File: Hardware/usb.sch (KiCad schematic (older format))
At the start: 13 parts

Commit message: Selected some footprints
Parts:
- P?: footprint (none) -> Connector_USB:USB_C_Receptacle_GCT_USB4085
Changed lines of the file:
@@
 F 0 "P?" H 3857 4567 50  0000 C CNN
 F 1 "USB_C_Plug_USB2.0" H 3857 4476 50  0000 C CNN
-F 2 "" H 3900 3700 50  0001 C CNN
+F 2 "Connector_USB:USB_C_Receptacle_GCT_USB4085" H 3900 3700 50  0001 C CNN
 F 3 "https://www.usb.org/sites/default/files/documents/usb_type-c.zip" H 3900 3700 50  0001 C CNN
 	1    3750 3700

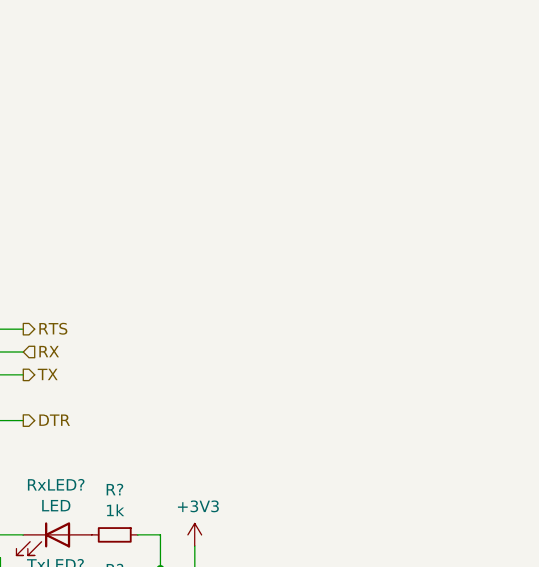
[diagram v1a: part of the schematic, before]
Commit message: Added test points everywhere
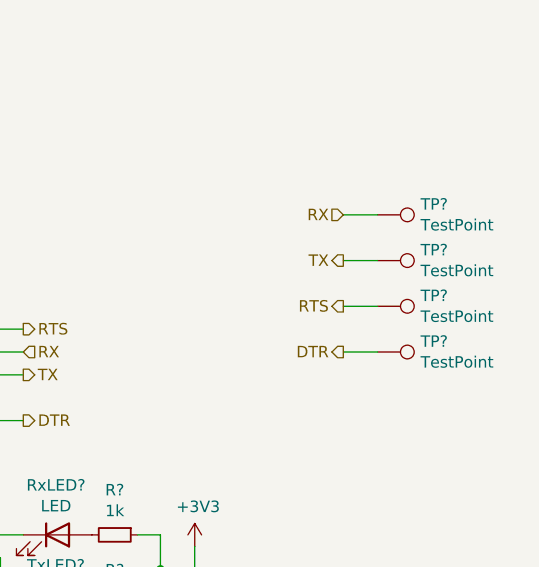
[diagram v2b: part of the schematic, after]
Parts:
- added TP? (x4): TestPoint, symbol Connector:TestPoint
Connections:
- net DTR: now also TP?.1
- net RTS: now also TP?.1
- net RX: now also TP?.1
- net TX: now also TP?.1
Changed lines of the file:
@@
 $Descr A4 11693 8268
 encoding utf-8
-Sheet 4 4
+Sheet 4 5
 Title ""
 Date ""
@@
 Text HLabel 7650 3750 2    50   Output ~ 0
 DTR
+$Comp
+L Connector:TestPoint TP?
+U 1 1 607C08D3
+P 9200 2850
+F 0 "TP?" V 9154 3038 50  0000 L CNN
+F 1 "TestPoint" V 9245 3038 50  0000 L CNN
+F 2 "" H 9400 2850 50  0001 C CNN
+F 3 "~" H 9400 2850 50  0001 C CNN
+	1    9200 2850
+	0    1    1    0
+$EndComp
+$Comp
+L Connector:TestPoint TP?
+U 1 1 607C0C71
+P 9200 3050
+F 0 "TP?" V 9154 3238 50  0000 L CNN
+F 1 "TestPoint" V 9245 3238 50  0000 L CNN
+F 2 "" H 9400 3050 50  0001 C CNN
+F 3 "~" H 9400 3050 50  0001 C CNN
+	1    9200 3050
+	0    1    1    0
+$EndComp
+Wire Wire Line
+	9200 2850 9050 2850
+Wire Wire Line
+	9200 3050 9050 3050
+$Comp
+L Connector:TestPoint TP?
+U 1 1 607C5A06
+P 9200 3250
+F 0 "TP?" V 9154 3438 50  0000 L CNN
+F 1 "TestPoint" V 9245 3438 50  0000 L CNN
+F 2 "" H 9400 3250 50  0001 C CNN
+F 3 "~" H 9400 3250 50  0001 C CNN
+	1    9200 3250
+	0    1    1    0
+$EndComp
+Wire Wire Line
+	9200 3250 9050 3250
+$Comp
+L Connector:TestPoint TP?
+U 1 1 607C6B8E
+P 9200 3450
+F 0 "TP?" V 9154 3638 50  0000 L CNN
+F 1 "TestPoint" V 9245 3638 50  0000 L CNN
+F 2 "" H 9400 3450 50  0001 C CNN
+F 3 "~" H 9400 3450 50  0001 C CNN
+	1    9200 3450
+	0    1    1    0
+$EndComp
+Wire Wire Line
+	9200 3450 9050 3450
+Text HLabel 9050 2850 0    50   Input ~ 0
+RX
+Text HLabel 9050 3050 0    50   Output ~ 0
+TX
+Text HLabel 9050 3250 0    50   Output ~ 0
+RTS
+Text HLabel 9050 3450 0    50   Output ~ 0
+DTR
 $EndSCHEMATC
